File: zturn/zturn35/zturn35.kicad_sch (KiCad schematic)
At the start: 50 parts, among them U1 74AXP4T245, U10 74AXP4T245, U11 74AXP4T245, U12 74AXP4T245, U2 74AXP4T245, U3 74AXP4T245, U4 74AXP4T245, U5 74AXP4T245, U6 74AXP4T245, U7 74AXP4T245, U8 74AXP4T245, U9 74AXP4T245

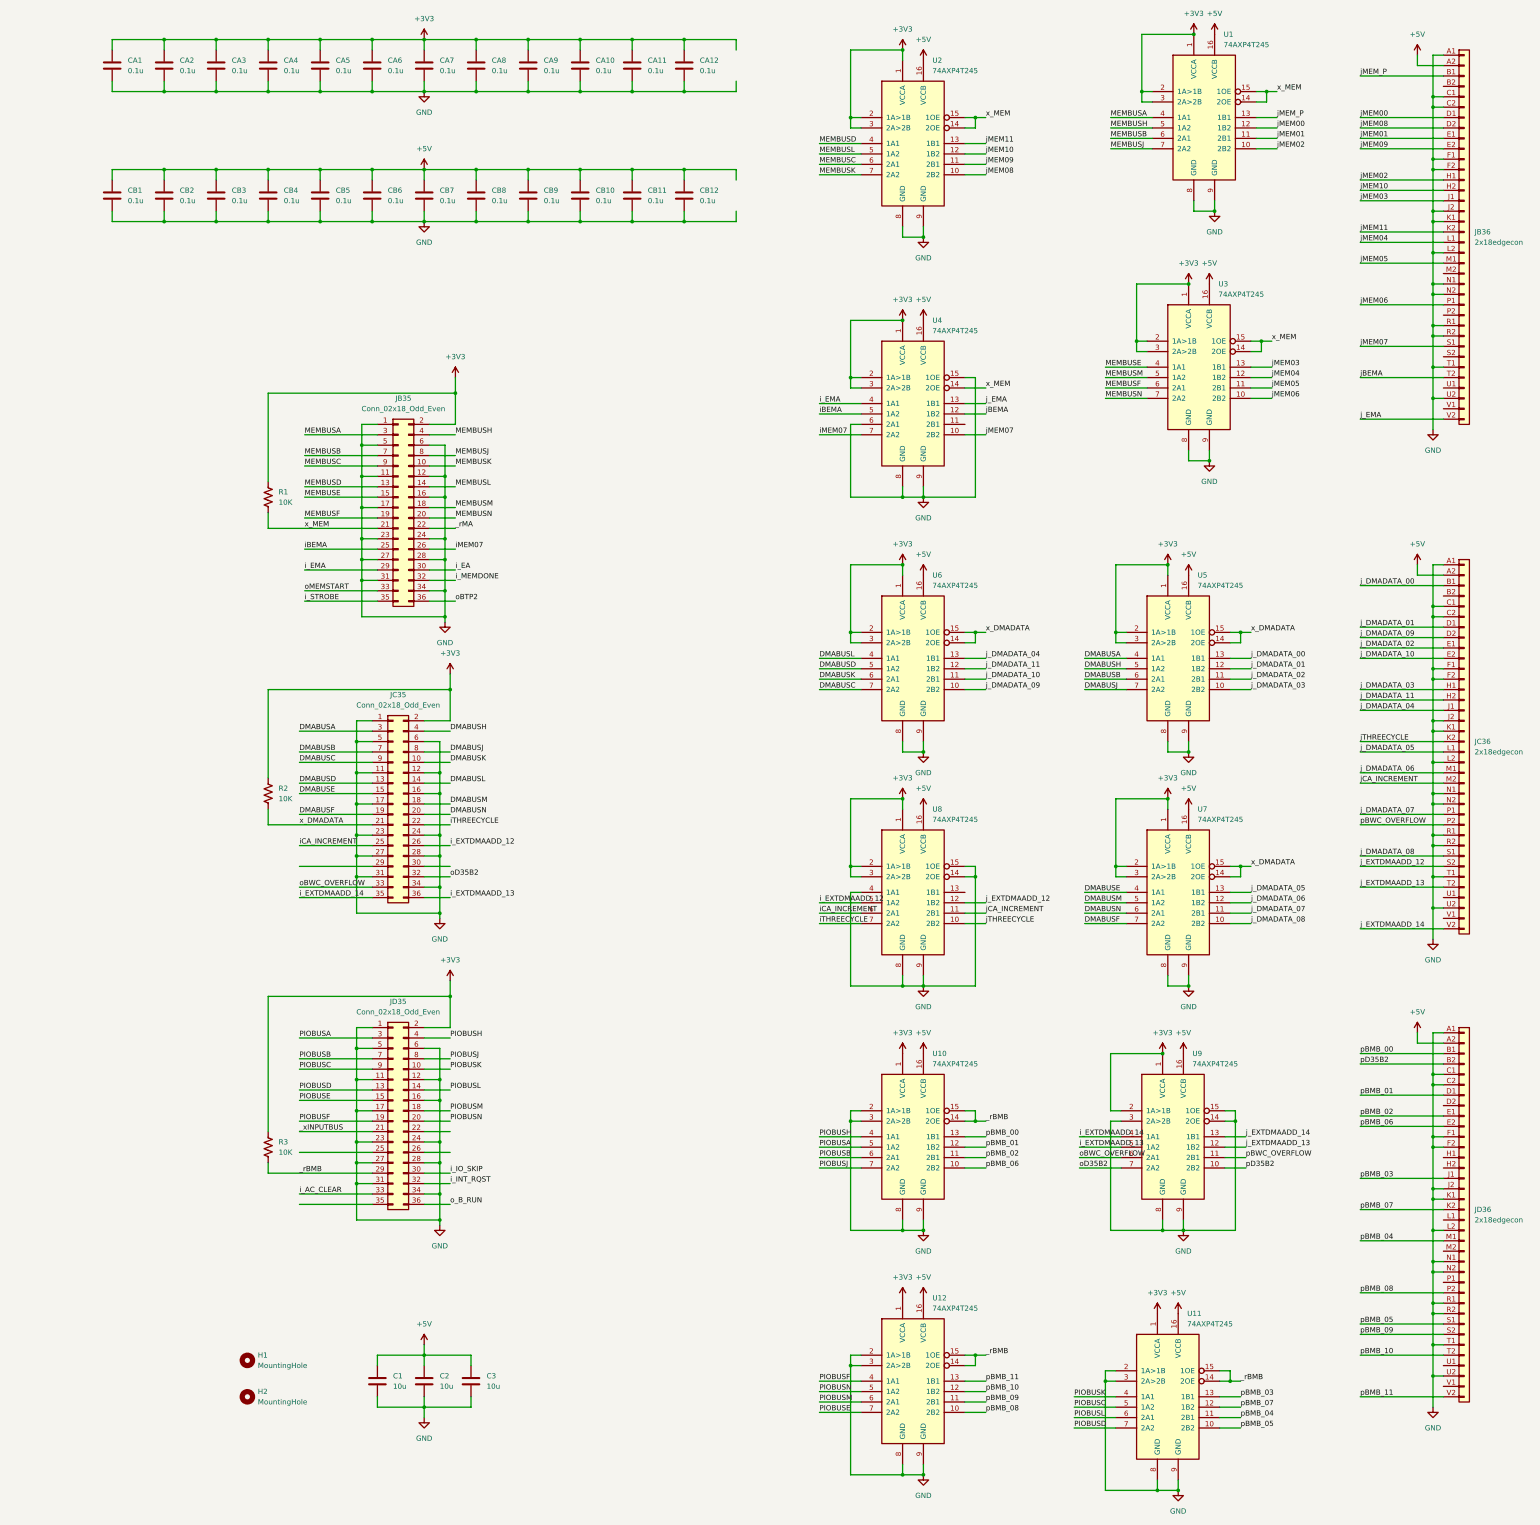
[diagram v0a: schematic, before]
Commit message: update zturn34,35 pcbs - move 10uF caps, add fiducials
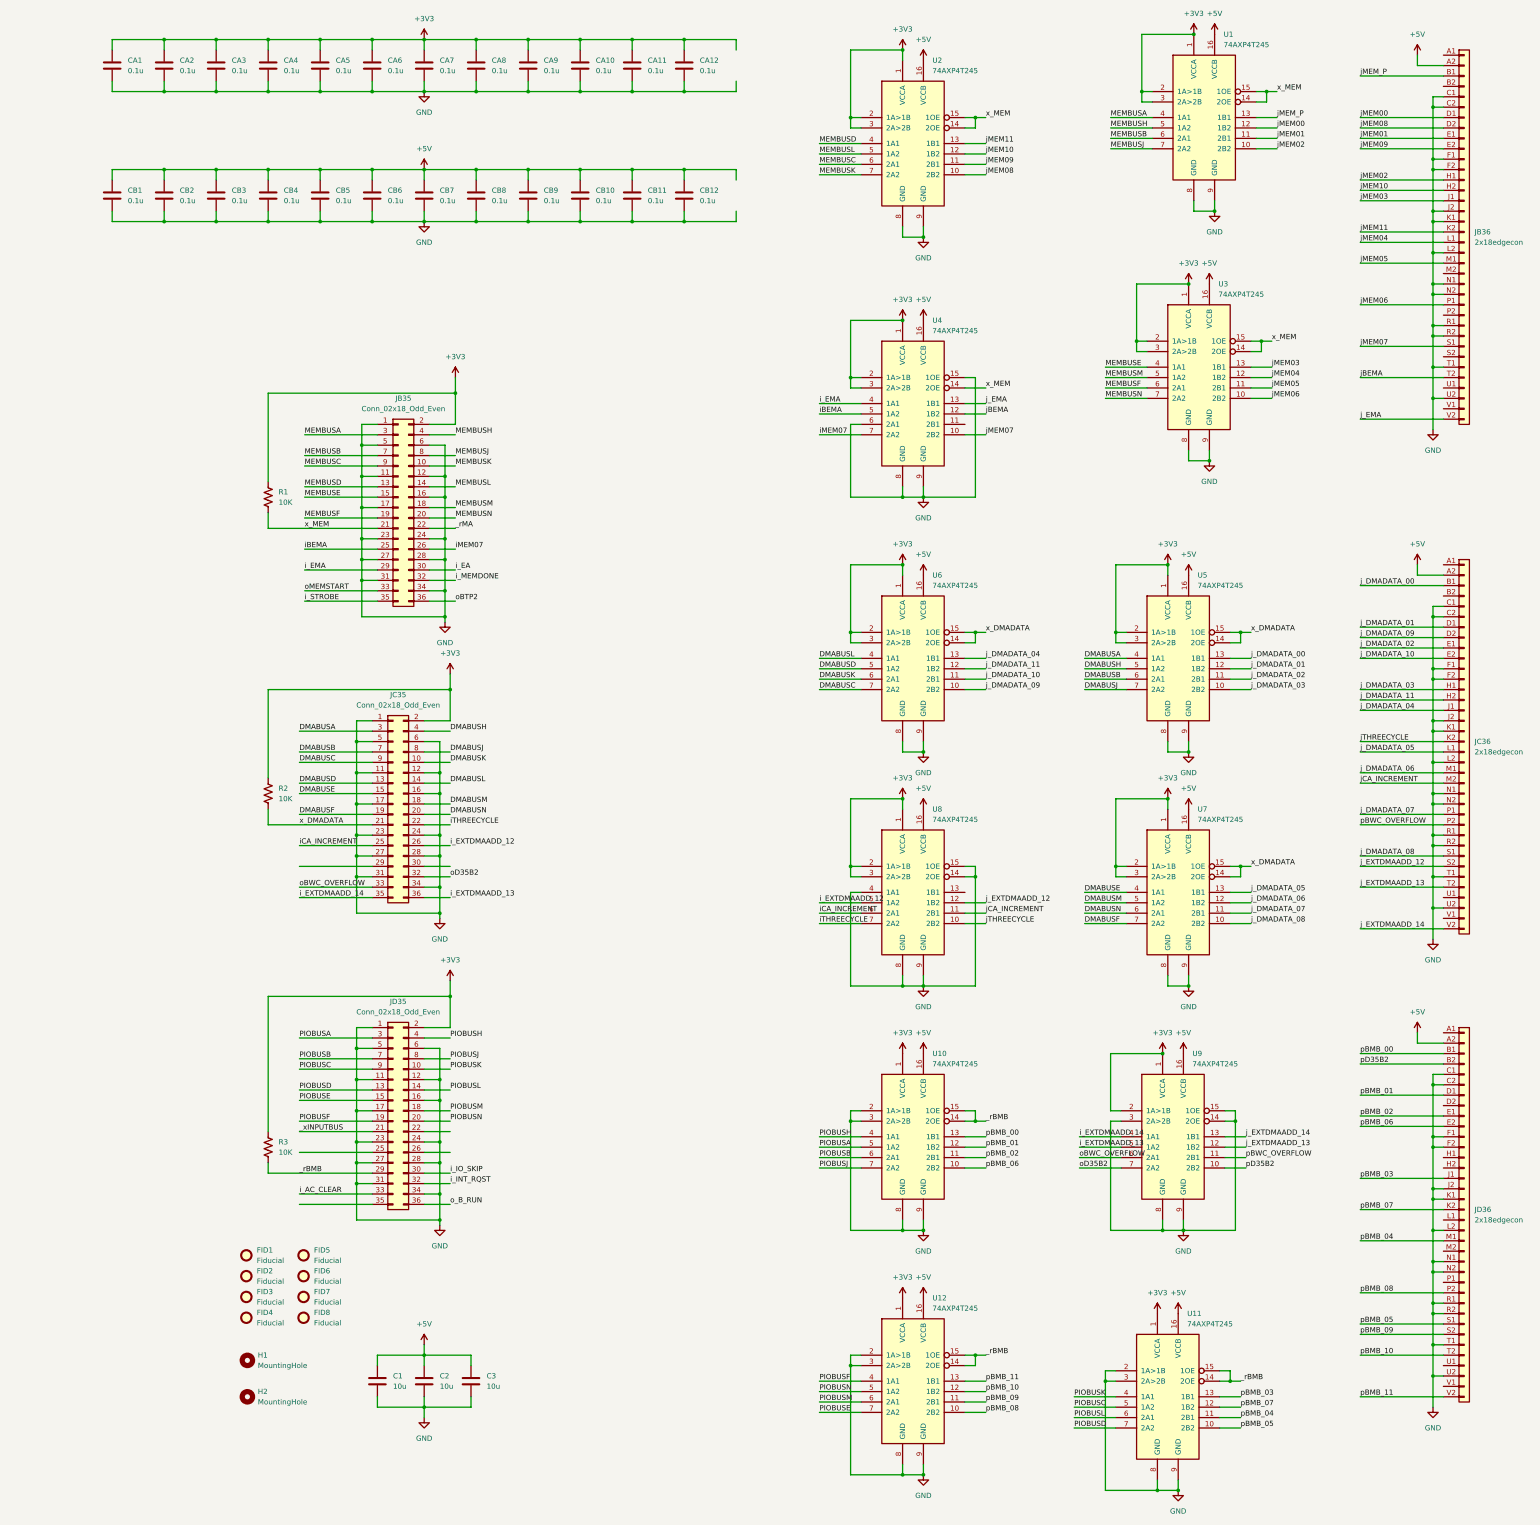
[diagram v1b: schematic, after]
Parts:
- added FID1, FID2, FID3, FID4, FID5, FID6, FID7, FID8: Fiducial, Fiducial:Fiducial_1mm_Mask2mm, symbol Mechanical:Fiducial
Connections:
- net GND: no longer JB36.A1, JC36.A1, JD36.A1
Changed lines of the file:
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@@
   (junction (at 266.7 19.05) (diameter 0) (color 0 0 0 0)
   )
-  (junction (at 576.58 33.02) (diameter 0) (color 0 0 0 0)
-  )
   (junction (at 292.1 63.5) (diameter 0) (color 0 0 0 0)
   )
   (junction (at 434.34 283.21) (diameter 0) (color 0 0 0 0)
   )
-  (junction (at 576.58 271.78) (diameter 0) (color 0 0 0 0)
-  )
   (junction (at 314.96 133.35) (diameter 0) (color 0 0 0 0)
   )
-  (junction (at 576.58 157.48) (diameter 0) (color 0 0 0 0)
-  )
   (junction (at 521.97 121.92) (diameter 0) (color 0 0 0 0)
   )
@@
     (stroke (width 0) (type default))
   )
-  (wire (pts (xy 576.58 22.86) (xy 579.12 22.86))
-    (stroke (width 0) (type default))
-  )
   (wire (pts (xy 393.7 31.75) (xy 406.4 31.75))
     (stroke (width 0) (type default))
@@
     (stroke (width 0) (type default))
   )
-  (wire (pts (xy 576.58 157.48) (xy 576.58 147.32))
-    (stroke (width 0) (type default))
-  )
   (wire (pts (xy 318.77 340.36) (xy 330.2 340.36))
     (stroke (width 0) (type default))
@@
     (stroke (width 0) (type default))
   )
-  (wire (pts (xy 576.58 147.32) (xy 579.12 147.32))
-    (stroke (width 0) (type default))
-  )
   (wire (pts (xy 434.34 342.9) (xy 436.88 342.9))
     (stroke (width 0) (type default))
@@
     (stroke (width 0) (type default))
   )
-  (wire (pts (xy 576.58 271.78) (xy 576.58 261.62))
-    (stroke (width 0) (type default))
-  )
   (wire (pts (xy 447.04 130.81) (xy 434.34 130.81))
     (stroke (width 0) (type default))
@@
     (stroke (width 0) (type default))
   )
-  (wire (pts (xy 576.58 261.62) (xy 579.12 261.62))
-    (stroke (width 0) (type default))
-  )
   (wire (pts (xy 532.13 99.06) (xy 537.21 99.06))
     (stroke (width 0) (type default))
@@
     (stroke (width 0) (type default))
   )
-  (wire (pts (xy 576.58 33.02) (xy 576.58 22.86))
-    (stroke (width 0) (type default))
-  )
   (wire (pts (xy 313.69 280.67) (xy 317.5 280.67))
     (stroke (width 0) (type default))
@@
     )
   )
+  (symbol (lib_id "Mechanical:Fiducial") (at 286.766 321.056 0) (unit 1)
+    (in_bom yes) (on_board yes) (dnp no) (fields_autoplaced)
+    (property "Reference" "FID2" (at 289.306 319.786 0)
+      (effects (font (size 1.27 1.27)) (justify left))
+    )
+    (property "Value" "Fiducial" (at 289.306 322.326 0)
+      (effects (font (size 1.27 1.27)) (justify left))
+    )
+    (property "Footprint" "Fiducial:Fiducial_1mm_Mask2mm" (at 286.766 321.056 0)
+      (effects (font (size 1.27 1.27)) hide)
+    )
+    (property "Datasheet" "~" (at 286.766 321.056 0)
+      (effects (font (size 1.27 1.27)) hide)
+    )
+    (instances
+      (project "zturn35"
+        (path "/f88ff33f-ea83-4481-9378-71bec9a888d0"
+          (reference "FID2") (unit 1)
+        )
+      )
+    )
+  )
   (symbol (lib_id "Device:C") (at 342.9 25.4 0) (unit 1)
     (in_bom yes) (on_board yes) (dnp no) (fields_autoplaced)
@@
     )
   )
+  (symbol (lib_id "Mechanical:Fiducial") (at 300.736 321.056 0) (unit 1)
+    (in_bom yes) (on_board yes) (dnp no) (fields_autoplaced)
+    (property "Reference" "FID6" (at 303.276 319.786 0)
+      (effects (font (size 1.27 1.27)) (justify left))
+    )
+    (property "Value" "Fiducial" (at 303.276 322.326 0)
+      (effects (font (size 1.27 1.27)) (justify left))
+    )
+    (property "Footprint" "Fiducial:Fiducial_1mm_Mask2mm" (at 300.736 321.056 0)
+      (effects (font (size 1.27 1.27)) hide)
+    )
+    (property "Datasheet" "~" (at 300.736 321.056 0)
+      (effects (font (size 1.27 1.27)) hide)
+    )
+    (instances
+      (project "zturn35"
+        (path "/f88ff33f-ea83-4481-9378-71bec9a888d0"
+          (reference "FID6") (unit 1)
+        )
+      )
+    )
+  )
   (symbol (lib_id "Device:C") (at 355.6 25.4 0) (unit 1)
     (in_bom yes) (on_board yes) (dnp no) (fields_autoplaced)
@@
     )
   )
+  (symbol (lib_id "Mechanical:Fiducial") (at 286.766 315.976 0) (unit 1)
+    (in_bom yes) (on_board yes) (dnp no) (fields_autoplaced)
+    (property "Reference" "FID1" (at 289.306 314.706 0)
+      (effects (font (size 1.27 1.27)) (justify left))
+    )
+    (property "Value" "Fiducial" (at 289.306 317.246 0)
+      (effects (font (size 1.27 1.27)) (justify left))
+    )
+    (property "Footprint" "Fiducial:Fiducial_1mm_Mask2mm" (at 286.766 315.976 0)
+      (effects (font (size 1.27 1.27)) hide)
+    )
+    (property "Datasheet" "~" (at 286.766 315.976 0)
+      (effects (font (size 1.27 1.27)) hide)
+    )
+    (instances
+      (project "zturn35"
+        (path "/f88ff33f-ea83-4481-9378-71bec9a888d0"
+          (reference "FID1") (unit 1)
+        )
+      )
+    )
+  )
   (symbol (lib_id "Device:C") (at 279.4 57.15 0) (unit 1)
     (in_bom yes) (on_board yes) (dnp no) (fields_autoplaced)
@@
     )
   )
+  (symbol (lib_id "Mechanical:Fiducial") (at 286.766 331.216 0) (unit 1)
+    (in_bom yes) (on_board yes) (dnp no) (fields_autoplaced)
+    (property "Reference" "FID4" (at 289.306 329.946 0)
+      (effects (font (size 1.27 1.27)) (justify left))
+    )
+    (property "Value" "Fiducial" (at 289.306 332.486 0)
+      (effects (font (size 1.27 1.27)) (justify left))
+    )
+    (property "Footprint" "Fiducial:Fiducial_1mm_Mask2mm" (at 286.766 331.216 0)
+      (effects (font (size 1.27 1.27)) hide)
+    )
+    (property "Datasheet" "~" (at 286.766 331.216 0)
+      (effects (font (size 1.27 1.27)) hide)
+    )
+    (instances
+      (project "zturn35"
+        (path "/f88ff33f-ea83-4481-9378-71bec9a888d0"
+          (reference "FID4") (unit 1)
+        )
+      )
+    )
+  )
   (symbol (lib_id "Device:R_US") (at 292.1 289.56 0) (unit 1)
     (in_bom yes) (on_board yes) (dnp no) (fields_autoplaced)
@@
     )
   )
+  (symbol (lib_id "Mechanical:Fiducial") (at 300.736 326.136 0) (unit 1)
+    (in_bom yes) (on_board yes) (dnp no) (fields_autoplaced)
+    (property "Reference" "FID7" (at 303.276 324.866 0)
+      (effects (font (size 1.27 1.27)) (justify left))
+    )
+    (property "Value" "Fiducial" (at 303.276 327.406 0)
+      (effects (font (size 1.27 1.27)) (justify left))
+    )
+    (property "Footprint" "Fiducial:Fiducial_1mm_Mask2mm" (at 300.736 326.136 0)
+      (effects (font (size 1.27 1.27)) hide)
+    )
+    (property "Datasheet" "~" (at 300.736 326.136 0)
+      (effects (font (size 1.27 1.27)) hide)
+    )
+    (instances
+      (project "zturn35"
+        (path "/f88ff33f-ea83-4481-9378-71bec9a888d0"
+          (reference "FID7") (unit 1)
+        )
+      )
+    )
+  )
   (symbol (lib_id "power:GND") (at 576.58 114.3 0) (unit 1)
     (in_bom yes) (on_board yes) (dnp no) (fields_autoplaced)
@@
     )
   )
+  (symbol (lib_id "Mechanical:Fiducial") (at 286.766 326.136 0) (unit 1)
+    (in_bom yes) (on_board yes) (dnp no) (fields_autoplaced)
+    (property "Reference" "FID3" (at 289.306 324.866 0)
+      (effects (font (size 1.27 1.27)) (justify left))
+    )
+    (property "Value" "Fiducial" (at 289.306 327.406 0)
+      (effects (font (size 1.27 1.27)) (justify left))
+    )
+    (property "Footprint" "Fiducial:Fiducial_1mm_Mask2mm" (at 286.766 326.136 0)
+      (effects (font (size 1.27 1.27)) hide)
+    )
+    (property "Datasheet" "~" (at 286.766 326.136 0)
+      (effects (font (size 1.27 1.27)) hide)
+    )
+    (instances
+      (project "zturn35"
+        (path "/f88ff33f-ea83-4481-9378-71bec9a888d0"
+          (reference "FID3") (unit 1)
+        )
+      )
+    )
+  )
   (symbol (lib_id "power:GND") (at 515.62 309.88 0) (unit 1)
     (in_bom yes) (on_board yes) (dnp no) (fields_autoplaced)
@@
     )
   )
+  (symbol (lib_id "Mechanical:Fiducial") (at 300.736 315.976 0) (unit 1)
+    (in_bom yes) (on_board yes) (dnp no) (fields_autoplaced)
+    (property "Reference" "FID5" (at 303.276 314.706 0)
+      (effects (font (size 1.27 1.27)) (justify left))
+    )
+    (property "Value" "Fiducial" (at 303.276 317.246 0)
+      (effects (font (size 1.27 1.27)) (justify left))
+    )
+    (property "Footprint" "Fiducial:Fiducial_1mm_Mask2mm" (at 300.736 315.976 0)
+      (effects (font (size 1.27 1.27)) hide)
+    )
+    (property "Datasheet" "~" (at 300.736 315.976 0)
+      (effects (font (size 1.27 1.27)) hide)
+    )
+    (instances
+      (project "zturn35"
+        (path "/f88ff33f-ea83-4481-9378-71bec9a888d0"
+          (reference "FID5") (unit 1)
+        )
+      )
+    )
+  )
   (symbol (lib_id "Device:R_US") (at 292.1 130.81 0) (unit 1)
     (in_bom yes) (on_board yes) (dnp no) (fields_autoplaced)
@@
         )
       )
+    )
+  )
+  (symbol (lib_id "Mechanical:Fiducial") (at 300.736 331.216 0) (unit 1)
+    (in_bom yes) (on_board yes) (dnp no) (fields_autoplaced)
+    (property "Reference" "FID8" (at 303.276 329.946 0)
+      (effects (font (size 1.27 1.27)) (justify left))
+    )
+    (property "Value" "Fiducial" (at 303.276 332.486 0)
+      (effects (font (size 1.27 1.27)) (justify left))
+    )
+    (property "Footprint" "Fiducial:Fiducial_1mm_Mask2mm" (at 300.736 331.216 0)
+      (effects (font (size 1.27 1.27)) hide)
+    )
+    (property "Datasheet" "~" (at 300.736 331.216 0)
+      (effects (font (size 1.27 1.27)) hide)
+    )
+    (instances
+      (project "zturn35"
+        (path "/f88ff33f-ea83-4481-9378-71bec9a888d0"
+          (reference "FID8") (unit 1)
+        )
+      )
